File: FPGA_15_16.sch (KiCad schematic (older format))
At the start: 24 parts, among them J15 10029449-111RLF, Q20 BSS139, Q21 BSS139, U1 XC7A100T-2FGG484C, U12 MC78L05ACDR2G, U42 SN65MLVD2DRBT

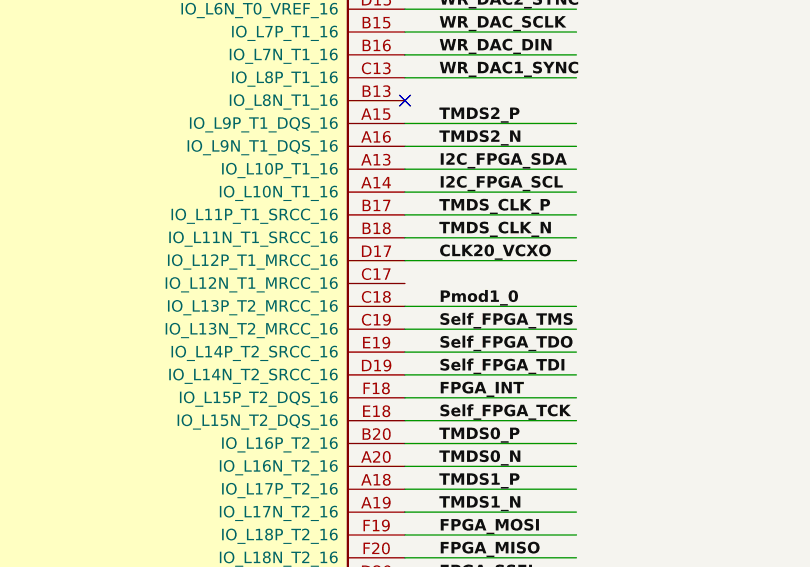
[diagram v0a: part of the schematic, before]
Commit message: README edited, less ERC errors and warnings
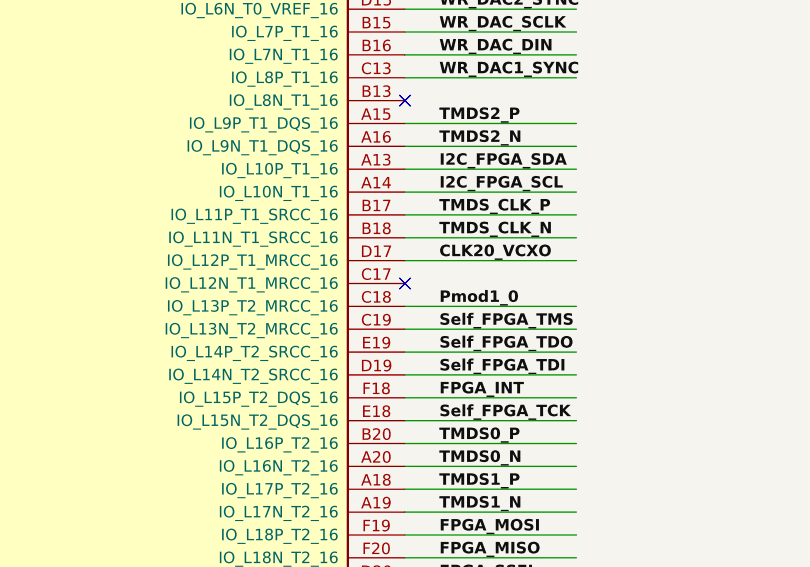
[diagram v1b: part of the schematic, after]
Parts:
- U42: Manufacturer Part Number (none) -> SN65MLVD2DRBT; PN SN65MLVD2DRBT -> (none)
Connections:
- no-connect marks 11 -> 12
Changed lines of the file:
@@
 F 2 "ICs And Semiconductors SMD:SON50P300X300X80-9N-R175X248" H 10800 5600 50  0001 C CNN
 F 3 "" H 10800 5600 50  0001 C CNN
-F 4 "SN65MLVD2DRBT" H 11050 5773 50  0001 C CNN "PN"
+F 4 "SN65MLVD2DRBT" H 11050 5773 50  0001 C CNN "Manufacturer Part Number"
 F 5 "-standalone" H 11050 5150 50  0001 C CNN "config"
 	1    10600 5700
@@
 Wire Wire Line
 	9250 5900 10600 5900
+NoConn ~ 9250 4200
 Wire Bus Line
 	14050 7300 14050 7600

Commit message: applied all required amendments to the project
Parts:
- Q20, Q21: value BSS139 -> BSS138LT1G; footprint SOT95P240X110-3N -> ICs And Semiconductors SMD:SOT95P240X110-3N; symbol Transistors:BSS139 -> Transistors:BSS138LT1G; Comment =Device -> BSS138LT1G; ComponentHeight 1.1mm -> 1.11mm; ComponentLink1Description ~~ -> (none); ComponentLink2Description ~~ -> (none); CreateDate 09/23/14 00:00:00 -> 03/23/09 00:00:00; Database Table Name (none) -> Transistors; Device BSS139 -> BSS138LT1G; Footprint Library (none) -> ICs And Semiconductors SMD; LatestRevisionDate 09/23/14 00:00:00 -> 03/23/09 00:00:00; Library Name ICs And Semiconductors SMD -> ICs And Semiconductors.DbLib; Manufacturer INFINEON -> ON SEMICONDUCTOR; Manufacturer Part Number BSS139H6327XTSA1 -> BSS138LT1G; Part Description 250V 30mA N-Channel SIPMOS® Small-Signal-Transistor -> 50V 200mA N-Channel Enhancement Mode Field-Effect Transistor; Part Number BSS139 -> BSS138LT1G; SCEM (none) -> (none); Sense Comment ~~ -> (none); Status ~~ -> (none); Status Comment ~~ -> (none)
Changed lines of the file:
@@
 EESchema Schematic File Version 4
 LIBS:AMC_FMC_Carrier-PcbDoc-cache
-EELAYER 29 0
+EELAYER 30 0
 EELAYER END
 $Descr A3 16535 11693
@@
 $EndComp
 $Comp
-L Transistors:BSS139 Q?
+L Transistors:BSS138LT1G Q?
 U 1 1 5D2E864A
 P 7250 9250
@@
 AR Path="/5C907554/5CAAC367/5D2E864A" Ref="Q20"  Part="1"
 F 0 "Q20" V 7614 9300 50  0000 C CNN
-F 1 "BSS139" V 7705 9300 50  0000 C CNN
-F 2 "SOT95P240X110-3N" H 7250 8040 60  0001 L CNN
+F 1 "BSS138LT1G" V 7705 9300 50  0000 C CNN
+F 2 "ICs And Semiconductors SMD:SOT95P240X110-3N" H 7250 8040 60  0001 L CNN
 F 3 "\\\\cern.ch\\dfs\\Applications\\Altium\\Datasheets\\BSS139.pdf" H 7250 8760 60  0001 L CNN
-F 4 "BSS139" H 7250 8670 60  0001 L CNN "Part Number"
+F 4 "BSS138LT1G" H 7250 8670 60  0001 L CNN "Part Number"
 F 5 "N-MOSFET-D 1G 2S 3D" H 7250 8580 60  0001 L CNN "Library Ref"
 F 6 "SchLib\\Transistors.SchLib" H 7250 8490 60  0001 L CNN "Library Path"
-F 7 "=Device" H 7250 8400 60  0001 L CNN "Comment"
+F 7 "BSS138LT1G" H 7250 8400 60  0001 L CNN "Comment"
 F 8 "Standard" H 7250 8310 60  0001 L CNN "Component Kind"
 F 9 "Standard" H 7250 8220 60  0001 L CNN "Component Type"
-F 10 "BSS139" H 7250 8130 60  0001 L CNN "Device"
+F 10 "BSS138LT1G" H 7250 8130 60  0001 L CNN "Device"
 F 11 "SOT23 3-Leads, Pitch 0.95mm - Body 1.4x3mm, IPC Medium Density" H 7250 7950 60  0001 L CNN "PackageDescription"
-F 12 "~~" H 7250 7860 60  0001 L CNN "Status"
-F 13 "250V 30mA N-Channel  SIPMOS® Small-Signal-Transistor" H 7250 7770 60  0001 L CNN "Part Description"
-F 14 "INFINEON" H 7250 7680 60  0001 L CNN "Manufacturer"
-F 15 "BSS139H6327XTSA1" H 7250 7590 60  0001 L CNN "Manufacturer Part Number"
+F 12 " " H 7250 7860 60  0001 L CNN "Status"
+F 13 "50V 200mA N-Channel Enhancement Mode Field-Effect Transistor" H 7250 7770 60  0001 L CNN "Part Description"
+F 14 "ON SEMICONDUCTOR" H 7250 7680 60  0001 L CNN "Manufacturer"
+F 15 "BSS138LT1G" H 7250 7590 60  0001 L CNN "Manufacturer Part Number"
 F 16 "3" H 7250 7500 60  0001 L CNN "Pin Count"
 F 17 "SOT23-3" H 7250 7410 60  0001 L CNN "Case"
@@
 F 21 "Yes" H 7250 7050 60  0001 L CNN "SMD"
 F 22 "No" H 7250 6960 60  0001 L CNN "Sense"
-F 23 "~~" H 7250 6870 60  0001 L CNN "Sense Comment"
+F 23 " " H 7250 6870 60  0001 L CNN "Sense Comment"
 F 24 "No" H 7250 6780 60  0001 L CNN "Bonding"
-F 25 "~~" H 7250 6690 60  0001 L CNN "Status Comment"
-F 26 "1.1mm" H 7250 6600 60  0001 L CNN "ComponentHeight"
+F 25 " " H 7250 6690 60  0001 L CNN "Status Comment"
+F 26 "1.11mm" H 7250 6600 60  0001 L CNN "ComponentHeight"
 F 27 "PcbLib\\ICs And Semiconductors SMD.PcbLib" H 7250 6510 60  0001 L CNN "Footprint Path"
 F 28 "SOT95P240X110-3N" H 7250 6420 60  0001 L CNN "Footprint Ref"
 F 29 "\\\\cern.ch\\dfs\\Applications\\Altium\\Datasheets\\BSS139.pdf" H 7250 6330 60  0001 L CNN "HelpURL"
 F 30 "~~" H 7250 6240 60  0001 L CNN "ComponentLink1URL"
-F 31 "~~" H 7250 6150 60  0001 L CNN "ComponentLink1Description"
+F 31 " " H 7250 6150 60  0001 L CNN "ComponentLink1Description"
 F 32 "~~" H 7250 6060 60  0001 L CNN "ComponentLink2URL"
-F 33 "~~" H 7250 5970 60  0001 L CNN "ComponentLink2Description"
+F 33 " " H 7250 5970 60  0001 L CNN "ComponentLink2Description"
 F 34 "CERN DEM JLC" H 7250 5880 60  0001 L CNN "Author"
-F 35 "09/23/14 00:00:00" H 7250 5790 60  0001 L CNN "CreateDate"
-F 36 "09/23/14 00:00:00" H 7250 5700 60  0001 L CNN "LatestRevisionDate"
-F 37 "ICs And Semiconductors SMD" H 7250 5610 60  0001 L CNN "Library Name"
+F 35 "03/23/09 00:00:00" H 7250 5790 60  0001 L CNN "CreateDate"
+F 36 "03/23/09 00:00:00" H 7250 5700 60  0001 L CNN "LatestRevisionDate"
+F 37 "ICs And Semiconductors.DbLib" H 7250 5610 60  0001 L CNN "Library Name"
 F 38 "This work is licensed under the Creative Commons CC-BY-SA 4.0 License. To the extent that circuit schematics that use Licensed Material can be considered to be ‘Adapted Material’, then the copyright holder waives article 3.b of the license with respect to these schematics." H 7250 5520 60  0001 L CNN "License"
+F 39 "Transistors" H 7250 9250 50  0001 C CNN "Database Table Name"
+F 40 "ICs And Semiconductors SMD" H 7250 9250 50  0001 C CNN "Footprint Library"
+F 41 " " H 7250 9250 50  0001 C CNN "SCEM"
 	1    7250 9250
 	0    1    1    0
 $EndComp
 $Comp
-L Transistors:BSS139 Q?
+L Transistors:BSS138LT1G Q?
 U 1 1 5D309024
 P 7250 10050
@@
 AR Path="/5C907554/5CAAC367/5D309024" Ref="Q21"  Part="1"
 F 0 "Q21" V 7614 10100 50  0000 C CNN
-F 1 "BSS139" V 7705 10100 50  0000 C CNN
-F 2 "SOT95P240X110-3N" H 7250 8840 60  0001 L CNN
+F 1 "BSS138LT1G" V 7705 10100 50  0000 C CNN
+F 2 "ICs And Semiconductors SMD:SOT95P240X110-3N" H 7250 8840 60  0001 L CNN
 F 3 "\\\\cern.ch\\dfs\\Applications\\Altium\\Datasheets\\BSS139.pdf" H 7250 9560 60  0001 L CNN
-F 4 "BSS139" H 7250 9470 60  0001 L CNN "Part Number"
+F 4 "BSS138LT1G" H 7250 9470 60  0001 L CNN "Part Number"
 F 5 "N-MOSFET-D 1G 2S 3D" H 7250 9380 60  0001 L CNN "Library Ref"
 F 6 "SchLib\\Transistors.SchLib" H 7250 9290 60  0001 L CNN "Library Path"
-F 7 "=Device" H 7250 9200 60  0001 L CNN "Comment"
+F 7 "BSS138LT1G" H 7250 9200 60  0001 L CNN "Comment"
 F 8 "Standard" H 7250 9110 60  0001 L CNN "Component Kind"
 F 9 "Standard" H 7250 9020 60  0001 L CNN "Component Type"
-F 10 "BSS139" H 7250 8930 60  0001 L CNN "Device"
+F 10 "BSS138LT1G" H 7250 8930 60  0001 L CNN "Device"
 F 11 "SOT23 3-Leads, Pitch 0.95mm - Body 1.4x3mm, IPC Medium Density" H 7250 8750 60  0001 L CNN "PackageDescription"
-F 12 "~~" H 7250 8660 60  0001 L CNN "Status"
-F 13 "250V 30mA N-Channel  SIPMOS® Small-Signal-Transistor" H 7250 8570 60  0001 L CNN "Part Description"
-F 14 "INFINEON" H 7250 8480 60  0001 L CNN "Manufacturer"
-F 15 "BSS139H6327XTSA1" H 7250 8390 60  0001 L CNN "Manufacturer Part Number"
+F 12 " " H 7250 8660 60  0001 L CNN "Status"
+F 13 "50V 200mA N-Channel Enhancement Mode Field-Effect Transistor" H 7250 8570 60  0001 L CNN "Part Description"
+F 14 "ON SEMICONDUCTOR" H 7250 8480 60  0001 L CNN "Manufacturer"
+F 15 "BSS138LT1G" H 7250 8390 60  0001 L CNN "Manufacturer Part Number"
 F 16 "3" H 7250 8300 60  0001 L CNN "Pin Count"
 F 17 "SOT23-3" H 7250 8210 60  0001 L CNN "Case"
@@
 F 21 "Yes" H 7250 7850 60  0001 L CNN "SMD"
 F 22 "No" H 7250 7760 60  0001 L CNN "Sense"
-F 23 "~~" H 7250 7670 60  0001 L CNN "Sense Comment"
+F 23 " " H 7250 7670 60  0001 L CNN "Sense Comment"
 F 24 "No" H 7250 7580 60  0001 L CNN "Bonding"
-F 25 "~~" H 7250 7490 60  0001 L CNN "Status Comment"
-F 26 "1.1mm" H 7250 7400 60  0001 L CNN "ComponentHeight"
+F 25 " " H 7250 7490 60  0001 L CNN "Status Comment"
+F 26 "1.11mm" H 7250 7400 60  0001 L CNN "ComponentHeight"
 F 27 "PcbLib\\ICs And Semiconductors SMD.PcbLib" H 7250 7310 60  0001 L CNN "Footprint Path"
 F 28 "SOT95P240X110-3N" H 7250 7220 60  0001 L CNN "Footprint Ref"
 F 29 "\\\\cern.ch\\dfs\\Applications\\Altium\\Datasheets\\BSS139.pdf" H 7250 7130 60  0001 L CNN "HelpURL"
 F 30 "~~" H 7250 7040 60  0001 L CNN "ComponentLink1URL"
-F 31 "~~" H 7250 6950 60  0001 L CNN "ComponentLink1Description"
+F 31 " " H 7250 6950 60  0001 L CNN "ComponentLink1Description"
 F 32 "~~" H 7250 6860 60  0001 L CNN "ComponentLink2URL"
-F 33 "~~" H 7250 6770 60  0001 L CNN "ComponentLink2Description"
+F 33 " " H 7250 6770 60  0001 L CNN "ComponentLink2Description"
 F 34 "CERN DEM JLC" H 7250 6680 60  0001 L CNN "Author"
-F 35 "09/23/14 00:00:00" H 7250 6590 60  0001 L CNN "CreateDate"
-F 36 "09/23/14 00:00:00" H 7250 6500 60  0001 L CNN "LatestRevisionDate"
-F 37 "ICs And Semiconductors SMD" H 7250 6410 60  0001 L CNN "Library Name"
+F 35 "03/23/09 00:00:00" H 7250 6590 60  0001 L CNN "CreateDate"
+F 36 "03/23/09 00:00:00" H 7250 6500 60  0001 L CNN "LatestRevisionDate"
+F 37 "ICs And Semiconductors.DbLib" H 7250 6410 60  0001 L CNN "Library Name"
 F 38 "This work is licensed under the Creative Commons CC-BY-SA 4.0 License. To the extent that circuit schematics that use Licensed Material can be considered to be ‘Adapted Material’, then the copyright holder waives article 3.b of the license with respect to these schematics." H 7250 6320 60  0001 L CNN "License"
+F 39 "Transistors" H 7250 10050 50  0001 C CNN "Database Table Name"
+F 40 "ICs And Semiconductors SMD" H 7250 10050 50  0001 C CNN "Footprint Library"
+F 41 " " H 7250 10050 50  0001 C CNN "SCEM"
 	1    7250 10050
 	0    1    1    0

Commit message: Rename library AMC_FMC_Carrier-PcbDoc-rescue as marble_misc
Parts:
- D10, D11: symbol AMC_FMC_Carrier-PcbDoc-rescue:HDMIULC6-4SC6-Diodes-AMC_FMC_Carrier-PcbDoc-rescue -> marble_misc:HDMIULC6-4SC6-Diodes-AMC_FMC_Carrier-PcbDoc-rescue
- J15: symbol AMC_FMC_Carrier-PcbDoc-rescue:SAMTEC_MHDMR-19-02-H-TH-L-TR-SAMTEC-AMC_FMC_Carrier-PcbDoc-rescue -> marble_misc:SAMTEC_MHDMR-19-02-H-TH-L-TR-SAMTEC-AMC_FMC_Carrier-PcbDoc-rescue
- U1: symbol AMC_FMC_Carrier-PcbDoc-rescue:XC7A200T-FBG484-FPGA_Xilinx_Artix7-AMC_FMC_Carrier-PcbDoc-rescue -> marble_misc:XC7A200T-FBG484-FPGA_Xilinx_Artix7-AMC_FMC_Carrier-PcbDoc-rescue
- U42: symbol AMC_FMC_Carrier-PcbDoc-rescue:SN65MLVD2DRBT-powerMG -> marble_misc:SN65MLVD2DRBT-powerMG
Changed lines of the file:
@@
 $EndComp
 $Comp
-L AMC_FMC_Carrier-PcbDoc-rescue:SAMTEC_MHDMR-19-02-H-TH-L-TR-SAMTEC-AMC_FMC_Carrier-PcbDoc-rescue J15
+L marble_misc:SAMTEC_MHDMR-19-02-H-TH-L-TR-SAMTEC-AMC_FMC_Carrier-PcbDoc-rescue J15
 U 1 1 5CBF72F4
 P 9750 7650
@@
 HDMI_HPD
 $Comp
-L AMC_FMC_Carrier-PcbDoc-rescue:HDMIULC6-4SC6-Diodes-AMC_FMC_Carrier-PcbDoc-rescue D10
+L marble_misc:HDMIULC6-4SC6-Diodes-AMC_FMC_Carrier-PcbDoc-rescue D10
 U 1 1 5C7A684D
 P 5550 8400
@@
 $EndComp
 $Comp
-L AMC_FMC_Carrier-PcbDoc-rescue:HDMIULC6-4SC6-Diodes-AMC_FMC_Carrier-PcbDoc-rescue D11
+L marble_misc:HDMIULC6-4SC6-Diodes-AMC_FMC_Carrier-PcbDoc-rescue D11
 U 1 1 5C854FB3
 P 5150 8750
@@
 	9250 5800 10050 5800
 $Comp
-L AMC_FMC_Carrier-PcbDoc-rescue:SN65MLVD2DRBT-powerMG U42
+L marble_misc:SN65MLVD2DRBT-powerMG U42
 U 1 1 5D20E21A
 P 10600 5700
@@
 Connection ~ 8350 1000
 $Comp
-L AMC_FMC_Carrier-PcbDoc-rescue:XC7A200T-FBG484-FPGA_Xilinx_Artix7-AMC_FMC_Carrier-PcbDoc-rescue U?
+L marble_misc:XC7A200T-FBG484-FPGA_Xilinx_Artix7-AMC_FMC_Carrier-PcbDoc-rescue U?
 U 2 1 5CB009EE
 P 7250 3900

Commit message: Strip extraneous AMC_FMC_Carrier-PcbDoc-rescue and powerMG from symbol names
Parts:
- D10, D11: symbol marble_misc:HDMIULC6-4SC6-Diodes-AMC_FMC_Carrier-PcbDoc-rescue -> marble_misc:HDMIULC6-4SC6-Diodes
- J15: symbol marble_misc:SAMTEC_MHDMR-19-02-H-TH-L-TR-SAMTEC-AMC_FMC_Carrier-PcbDoc-rescue -> marble_misc:SAMTEC_MHDMR-19-02-H-TH-L-TR-SAMTEC
- U1: symbol marble_misc:XC7A200T-FBG484-FPGA_Xilinx_Artix7-AMC_FMC_Carrier-PcbDoc-rescue -> marble_misc:XC7A200T-FBG484-FPGA_Xilinx_Artix7
- U42: symbol marble_misc:SN65MLVD2DRBT-powerMG -> marble_misc:SN65MLVD2DRBT
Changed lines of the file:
@@
 $EndComp
 $Comp
-L marble_misc:SAMTEC_MHDMR-19-02-H-TH-L-TR-SAMTEC-AMC_FMC_Carrier-PcbDoc-rescue J15
+L marble_misc:SAMTEC_MHDMR-19-02-H-TH-L-TR-SAMTEC J15
 U 1 1 5CBF72F4
 P 9750 7650
@@
 HDMI_HPD
 $Comp
-L marble_misc:HDMIULC6-4SC6-Diodes-AMC_FMC_Carrier-PcbDoc-rescue D10
+L marble_misc:HDMIULC6-4SC6-Diodes D10
 U 1 1 5C7A684D
 P 5550 8400
@@
 $EndComp
 $Comp
-L marble_misc:HDMIULC6-4SC6-Diodes-AMC_FMC_Carrier-PcbDoc-rescue D11
+L marble_misc:HDMIULC6-4SC6-Diodes D11
 U 1 1 5C854FB3
 P 5150 8750
@@
 	9250 5800 10050 5800
 $Comp
-L marble_misc:SN65MLVD2DRBT-powerMG U42
+L marble_misc:SN65MLVD2DRBT U42
 U 1 1 5D20E21A
 P 10600 5700
@@
 Connection ~ 8350 1000
 $Comp
-L marble_misc:XC7A200T-FBG484-FPGA_Xilinx_Artix7-AMC_FMC_Carrier-PcbDoc-rescue U?
+L marble_misc:XC7A200T-FBG484-FPGA_Xilinx_Artix7 U?
 U 2 1 5CB009EE
 P 7250 3900

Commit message: Symbols lib. and schematic: update footprint fields
sync with layout is now possible without errors
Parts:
- J15: footprint hdmi2usb:HDMI_TH -> Marble:10029449-111RLF; Field4 (none) -> HDMI; Manufacturer Part Number 10029449-111RLF -> MHDMR-19-02-H-TH-L-TR; Part Number 10029449-111RLF -> SAMTEC_MHDMR-19-02-H-TH-L-TR
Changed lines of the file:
@@
 F 0 "J15" H 10180 6500 50  0000 L CNN
 F 1 "10029449-111RLF" H 9750 5250 60  0001 L CNN
-F 2 "hdmi2usb:HDMI_TH" H 9750 4350 60  0001 L CNN
-F 3 "" H 9750 5070 60  0001 L CNN
+F 2 "Marble:10029449-111RLF" H 9750 4350 60  0001 L CNN
+F 3 "\\\\cern.ch\\dfs\\Applications\\Altium\\Datasheets\\SAMTEC_MHDMR-19-02-H-TH-L-TR.pdf" H 9750 5070 60  0001 L CNN
 F 4 "HDMI" H 9750 4980 60  0001 L CNN "Pole4"
-F 5 "10029449-111RLF" H 9750 4980 60  0001 L CNN "Part Number"
+F 5 "SAMTEC_MHDMR-19-02-H-TH-L-TR" H 9750 4980 60  0001 L CNN "Part Number"
 F 6 "Connector HDMI 19 Male + 1 Shield" H 9750 4890 60  0001 L CNN "Library Ref"
 F 7 "SchLib\\Connectors.SchLib" H 9750 4800 60  0001 L CNN "Library Path"
@@
 F 27 "19 Contacts, Pitch 0.4mm, Right Angle, Mini  HDMI High Speed I/O Receptacle" H 9750 2910 60  0001 L CNN "Part Description"
 F 28 "SAMTEC" H 9750 2820 60  0001 L CNN "Manufacturer"
-F 29 "10029449-111RLF" H 9750 2730 60  0001 L CNN "Manufacturer Part Number"
+F 29 "MHDMR-19-02-H-TH-L-TR" H 9750 2730 60  0001 L CNN "Manufacturer Part Number"
 F 30 "3.2mm" H 9750 2640 60  0001 L CNN "ComponentHeight"
 F 31 "\\\\cern.ch\\dfs\\Applications\\Altium\\Datasheets\\SAMTEC_MHDMR-19-02-H-TH-L-TR.pdf" H 9750 2550 60  0001 L CNN "HelpURL"
@@
 F 39 "SAMTEC SMD" H 9750 1830 60  0001 L CNN "Library Name"
 F 40 "This work is licensed under the Creative Commons CC-BY-SA 4.0 License. To the extent that circuit schematics that use Licensed Material can be considered to be ‘Adapted Material’, then the copyright holder waives article 3.b of the license with respect to these schematics." H 9750 1740 60  0001 L CNN "License"
+F 41 "HDMI" H 9750 7650 50  0001 C CNN "Field4"
 	1    9750 7650
 	1    0    0    -1
